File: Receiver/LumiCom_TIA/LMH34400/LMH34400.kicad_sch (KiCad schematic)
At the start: 24 parts, among them J1 TEST, J2 Conn_Coaxial, J3 Vout, J4 N_EN, J5 N_ALC, J6 Conn_Coaxial, U1 XLMH34400IDRLR

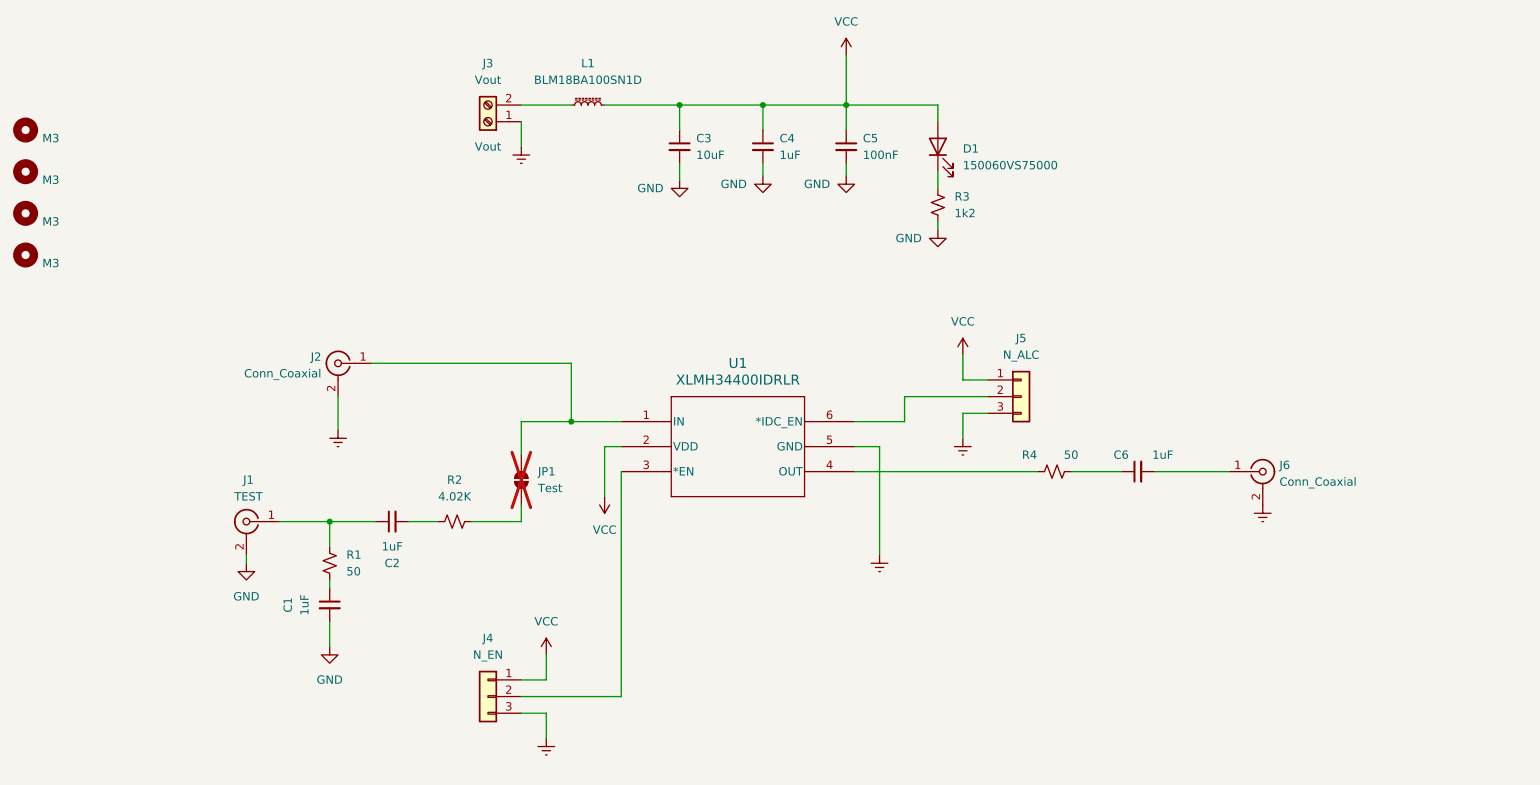
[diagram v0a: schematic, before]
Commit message: Multiple updates
SMA, Screw terminals, track widths, added some optional 0 ohm bypass resistors
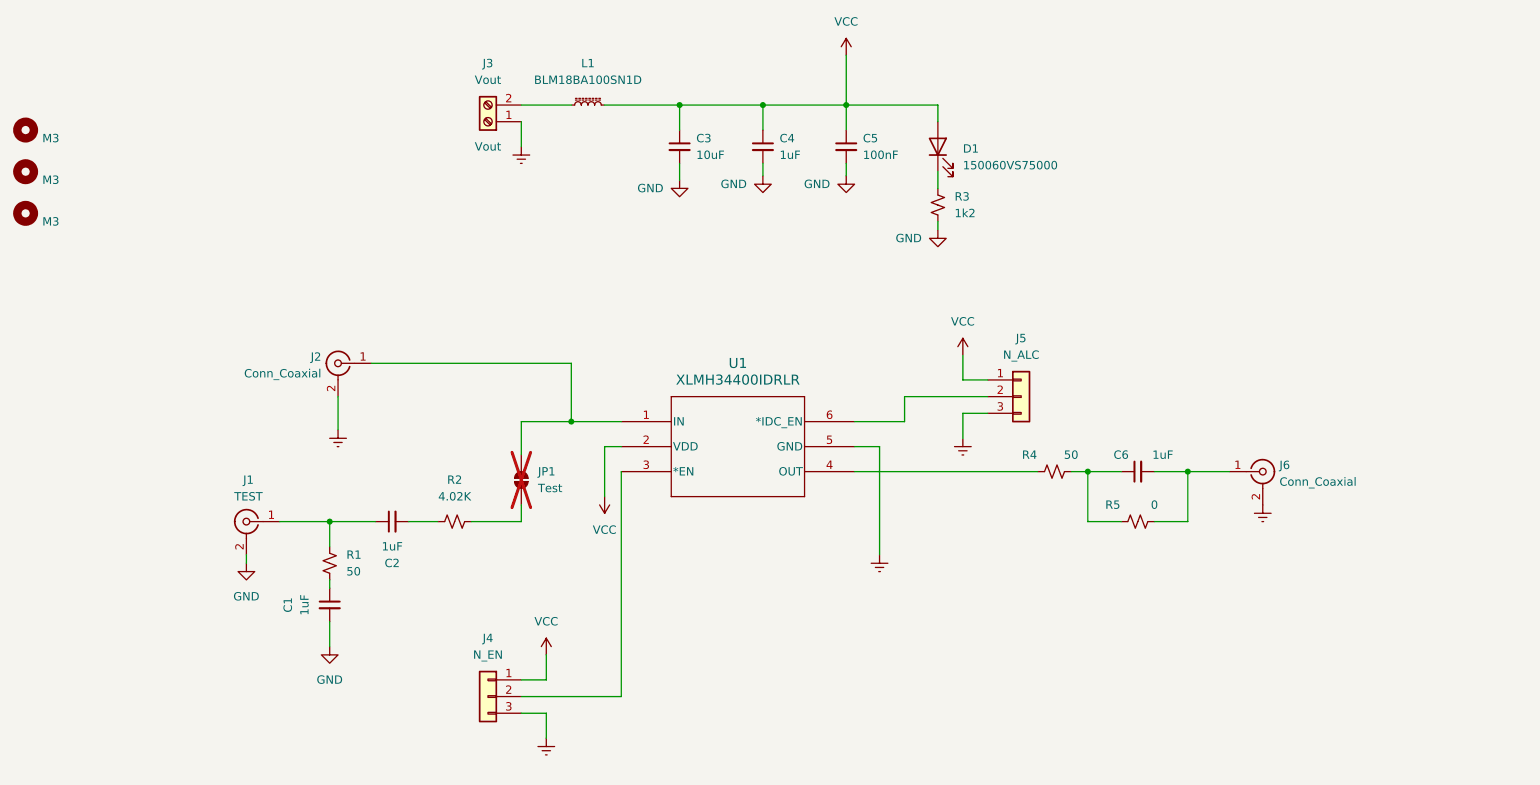
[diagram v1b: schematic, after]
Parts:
- removed H4: M3, MountingHole:MountingHole_3.2mm_M3_DIN965, symbol Mechanical:MountingHole
- added R5: 0, Resistor_SMD:R_0603_1608Metric_Pad0.98x0.95mm_HandSolder, symbol Device:R_Small_US
- J1, J2, J6: footprint LumiCom_TIA:RFSOLUTIONS_CON-SMA-EDGE-S -> Connector_Coaxial:SMA_Samtec_SMA-J-P-X-ST-EM1_EdgeMount
- J3: footprint TerminalBlock_Phoenix:TerminalBlock_Phoenix_MPT-0,5-2-2.54_1x02_P2.54mm_Horizontal -> TerminalBlock_Phoenix:TerminalBlock_Phoenix_MKDS-1,5-2_1x02_P5.00mm_Horizontal
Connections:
- net at C6.1, R4.2: now also R5.1
- net at C6.2, J6.1 (In): now also R5.2
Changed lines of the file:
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@@
 	)
 	(junction
+		(at 196.85 105.41)
+		(diameter 0)
+		(color 0 0 0 0)
+	)
+	(junction
 		(at 160.02 49.53)
 		(diameter 0)
 		(color 0 0 0 0)
 	)
+	(junction
+		(at 212.09 105.41)
+		(diameter 0)
+		(color 0 0 0 0)
+	)
 	(wire
 		(pts
@@
 	(wire
 		(pts
+			(xy 196.85 113.03) (xy 196.85 105.41)
+		)
+		(stroke
+			(width 0)
+			(type default)
+		)
+	)
+	(wire
+		(pts
 			(xy 134.62 49.53) (xy 134.62 53.34)
 		)
@@
 	(wire
 		(pts
+			(xy 207.01 113.03) (xy 212.09 113.03)
+		)
+		(stroke
+			(width 0)
+			(type default)
+		)
+	)
+	(wire
+		(pts
 			(xy 168.91 93.98) (xy 181.61 93.98)
 		)
@@
 	(wire
 		(pts
+			(xy 212.09 105.41) (xy 212.09 113.03)
+		)
+		(stroke
+			(width 0)
+			(type default)
+		)
+	)
+	(wire
+		(pts
 			(xy 110.49 113.03) (xy 102.87 113.03)
 		)
@@
 	(wire
 		(pts
+			(xy 196.85 105.41) (xy 201.93 105.41)
+		)
+		(stroke
+			(width 0)
+			(type default)
+		)
+	)
+	(wire
+		(pts
+			(xy 212.09 105.41) (xy 207.01 105.41)
+		)
+		(stroke
+			(width 0)
+			(type default)
+		)
+	)
+	(wire
+		(pts
 			(xy 110.49 52.07) (xy 110.49 55.88)
 		)
@@
 	(wire
 		(pts
+			(xy 201.93 113.03) (xy 196.85 113.03)
+		)
+		(stroke
+			(width 0)
+			(type default)
+		)
+	)
+	(wire
+		(pts
 			(xy 134.62 49.53) (xy 147.32 49.53)
 		)
@@
 	(wire
 		(pts
-			(xy 218.44 105.41) (xy 207.01 105.41)
+			(xy 218.44 105.41) (xy 212.09 105.41)
 		)
 		(stroke
@@
 	(wire
 		(pts
-			(xy 194.31 105.41) (xy 201.93 105.41)
+			(xy 194.31 105.41) (xy 196.85 105.41)
 		)
 		(stroke
@@
 	)
 	(symbol
+		(lib_id "Device:R_Small_US")
+		(at 204.47 113.03 90)
+		(unit 1)
+		(exclude_from_sim no)
+		(in_bom yes)
+		(on_board yes)
+		(dnp no)
+		(property "Reference" "R5"
+			(at 200.66 110.49 90)
+			(effects
+				(font
+					(size 1.27 1.27)
+				)
+			)
+		)
+		(property "Value" "0"
+			(at 207.01 110.49 90)
+			(effects
+				(font
+					(size 1.27 1.27)
+				)
+			)
+		)
+		(property "Footprint" "Resistor_SMD:R_0603_1608Metric_Pad0.98x0.95mm_HandSolder"
+			(at 204.47 113.03 0)
+			(effects
+				(font
+					(size 1.27 1.27)
+				)
+				(hide yes)
+			)
+		)
+		(property "Datasheet" "~"
+			(at 204.47 113.03 0)
+			(effects
+				(font
+					(size 1.27 1.27)
+				)
+				(hide yes)
+			)
+		)
+		(property "Description" "Resistor, small US symbol"
+			(at 204.47 113.03 0)
+			(effects
+				(font
+					(size 1.27 1.27)
+				)
+				(hide yes)
+			)
+		)
+		(pin "2"
+		)
+		(pin "1"
+		)
+		(instances
+			(project "LumiCom_TIA"
+				(path "/27381ed8-96e6-4041-ba7f-c08f9d949351/97796698-2adc-4146-98ed-b0bd6c43e980"
+					(reference "R5")
+					(unit 1)
+				)
+			)
+		)
+	)
+	(symbol
 		(lib_id "Device:C_Small")
 		(at 134.62 55.88 0)
@@
 			)
 		)
-		(property "Footprint" "LumiCom_TIA:RFSOLUTIONS_CON-SMA-EDGE-S"
+		(property "Footprint" "Connector_Coaxial:SMA_Samtec_SMA-J-P-X-ST-EM1_EdgeMount"
 			(at 82.55 88.9 0)
 			(effects
@@
 			)
 		)
-		(property "Footprint" "TerminalBlock_Phoenix:TerminalBlock_Phoenix_MPT-0,5-2-2.54_1x02_P2.54mm_Horizontal"
+		(property "Footprint" "TerminalBlock_Phoenix:TerminalBlock_Phoenix_MKDS-1,5-2_1x02_P5.00mm_Horizontal"
 			(at 105.41 52.07 0)
 			(effects
@@
 			)
 		)
-		(property "Footprint" "LumiCom_TIA:RFSOLUTIONS_CON-SMA-EDGE-S"
+		(property "Footprint" "Connector_Coaxial:SMA_Samtec_SMA-J-P-X-ST-EM1_EdgeMount"
 			(at 68.58 113.03 0)
 			(effects
@@
 			)
 		)
-		(property "Footprint" "LumiCom_TIA:RFSOLUTIONS_CON-SMA-EDGE-S"
+		(property "Footprint" "Connector_Coaxial:SMA_Samtec_SMA-J-P-X-ST-EM1_EdgeMount"
 			(at 223.52 105.41 0)
 			(effects
@@
 					(unit 1)
 				)
-			)
-		)
-	)
-	(symbol
-		(lib_id "Mechanical:MountingHole")
-		(at 34.925 72.39 0)
-		(unit 1)
-		(exclude_from_sim yes)
-		(in_bom no)
-		(on_board yes)
-		(dnp no)
-		(fields_autoplaced yes)
-		(property "Reference" "H4"
-			(at 37.465 71.1199 0)
-			(effects
-				(font
-					(size 1.27 1.27)
-				)
-				(justify left)
-				(hide yes)
-			)
-		)
-		(property "Value" "M3"
-			(at 37.465 73.6599 0)
-			(effects
-				(font
-					(size 1.27 1.27)
-				)
-				(justify left)
-			)
-		)
-		(property "Footprint" "MountingHole:MountingHole_3.2mm_M3_DIN965"
-			(at 34.925 72.39 0)
-			(effects
-				(font
-					(size 1.27 1.27)
-				)
-				(hide yes)
-			)
-		)
-		(property "Datasheet" "~"
-			(at 34.925 72.39 0)
-			(effects
-				(font
-					(size 1.27 1.27)
-				)
-				(hide yes)
-			)
-		)
-		(property "Description" "Mounting Hole without connection"
-			(at 34.925 72.39 0)
-			(effects
-				(font
-					(size 1.27 1.27)
-				)
-				(hide yes)
-			)
-		)
-		(instances
-			(project "LumiCom_TIA"
-				(path "/27381ed8-96e6-4041-ba7f-c08f9d949351/97796698-2adc-4146-98ed-b0bd6c43e980"
-					(reference "H4")
-					(unit 1)
-				)
